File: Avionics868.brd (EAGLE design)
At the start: 88.8 x 22.9 mm, 65 parts, among them SW1 B3U-1000P-2P-SMD, U1 ATSAMD21G18_QFN, U2 SPX3819M5-L-3-0, U3 MCP73831T-2ACI/OT, U4 MPU-9250, U5 SIM868, U6 BMP280, X1 JSTPH, X2 32.768, X3 ST-USB-001G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

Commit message: a ground via was unconnected
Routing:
- net GND: track 309.9 -> 310.7 mm
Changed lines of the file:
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@@
 <wire x1="46.5455" y1="11.43" x2="46.5045" y2="11.4325" width="0" layer="19" extent="1-1"/>
 <wire x1="17.399" y1="5.715" x2="17.526" y2="4.0005" width="0" layer="19" extent="1-1"/>
+<wire x1="2.413" y1="11.43" x2="1.5875" y2="11.43" width="0.8128" layer="1"/>
 </signal>
 <signal name="MOSI">

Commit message: Made lots of tweaks!
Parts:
- removed GPS_ANT, GSM_ANT: U-FL, Seeed-Connector -2016:U-FL3P-SMD-2.6X2.6X1.0MM
- added C25: 100nf, Seeed-Capacitor-2016:C0603
- added C26: 10nf, Seeed-Capacitor-2016:C0603
- added C27, C28, C29: 10uf, Seeed-Capacitor-2016:C0603
- added X5, X6: U-FL, Seeed-Connector -2016:U-FL3P-SMD-2.6X2.6X1.0MM
- C1, C14, C7: value 1uF -> 1uf; device microbuilder:0603-NO -> Seeed-Capacitor-2016:C0603
- C10, C11, C12, C13, C9: device Seeed-Capacitor-2016:C0402 -> Seeed-Capacitor-2016:C0603
- C15: device Seeed-Capacitor-2016:C0402 -> Custom:C0603
- C19, C22, C24: value 100nf -> 10nf; device Seeed-Capacitor-2016:C0402 -> Seeed-Capacitor-2016:C0603
- C2, C4: value 22pF -> 22pf; device microbuilder:0603-NO -> Seeed-Capacitor-2016:C0603
- C21, C23: value 10uf -> 100nf
- R3, R4, R5, R9: device Seeed-Resistor-2016:R0402 -> Seeed-Resistor-2016:R0603
- moved C24 113.9 mm to (-21.6, -15.2)
- moved C22 111.2 mm to (-21.6, -26.7), turned to 0 degrees
- moved C23 110.5 mm to (-21.6, -11.4), turned to 0 degrees
- moved C21 100.4 mm to (-21.6, -22.9)
- moved C20 29.3 mm to (65.7, 27.2), turned to 270 degrees
- moved U4 28.6 mm to (65.8, 30.1)
- moved C9 27.6 mm to (62.2, 27.9), turned to 90 degrees
- moved C10 27.1 mm to (62.2, 31.6), turned to 90 degrees
- moved C11 27.1 mm to (62.0, 29.9), turned to 90 degrees
- moved R4 19.9 mm to (56.5, 32.3)
- moved R5 19.5 mm to (53.3, 32.3)
- moved C13 18.8 mm to (53.2, 26.9)
- moved C19 18.8 mm to (55.4, 26.9)
- moved U6 18.8 mm to (54.4, 28.9)
- moved L2 10.0 mm to (38.2, 5.40), turned to 270 degrees
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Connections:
- net +3V: now also C20.2, C23.2, C27.2, C28.2; no longer C20.1, C23.1
- net GND: now also C20.1, C21.1, C23.1, C25.1, C26.1, C27.1, C28.1, C29.1, X5.GND1, X5.GND2, X6.GND1, X6.GND2; no longer C20.2, C21.2, C23.2, GPS_ANT.GND1, GPS_ANT.GND2, GSM_ANT.GND1, GSM_ANT.GND2
- net GPS_ANT: now also X6.D; no longer GPS_ANT.D
- net GSM_ANT: now also X5.D; no longer GSM_ANT.D
- net SIM_VDD: now also C21.2, C29.2; no longer C21.1
- net VBAT: now also C25.2, C26.2
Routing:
- net GND: track 310.7 -> 251.6 mm, vias 111 -> 66
- net TX5/GPS_RX: track 53.9 -> 25.0 mm
- net D7/SD_CS: track 81.2 -> 53.2 mm
- net GPS_EN: track 58.3 -> 33.0 mm
- net RX5/GPS_TX: track 50.1 -> 27.6 mm
- net +3V: track 172.0 -> 151.7 mm, vias 9 -> 12
- net !RESET: track 23.7 -> 11.4 mm
- net D4/TX2/GSM_RX: track 34.6 -> 22.3 mm
- net D9/VOLT: track 38.9 -> 26.6 mm, vias 5 -> 3
- net SCL: track 41.3 -> 30.7 mm, vias 2 -> 1
- net D3/RX2/GSM_TX: track 33.9 -> 29.9 mm
- net RTS2: track 38.4 -> 34.5 mm
- net SDA: track 40.9 -> 37.6 mm, vias 3 -> 1
- net PWRKEY: track 31.3 -> 28.1 mm
- net D5/CTS2: track 29.8 -> 26.8 mm
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- added copper zone on layer 16, net +3V
- removed copper zone on layer 1, net VBAT
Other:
- board size 88.8 x 22.9 mm -> 86.4 x 22.9 mm

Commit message: LOTS of tweaks. No more 403s.
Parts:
- removed C27: 10uf, Seeed-Capacitor-2016:C0603
- moved C28 103.8 mm to (80.0, 2.10), turned to 180 degrees
- moved C29 101.2 mm to (66.0, 20.3)
- moved C21 101.2 mm to (69.9, 20.3)
- moved C22 101.1 mm to (67.9, 20.3)
- moved C23 100.6 mm to (78.1, 2.10), turned to 180 degrees
- moved C24 99.3 mm to (76.2, 2.10), turned to 180 degrees
- moved C26 64.8 mm to (46.1, 11.4), turned to 90 degrees
- moved C25 58.2 mm to (41.7, 18.8), turned to 180 degrees
- moved C11 30.4 mm to (36.1, 13.9)
- moved C10 30.0 mm to (36.8, 15.6)
- moved U4 29.6 mm to (40.8, 14.4)
- moved C20 29.2 mm to (41.1, 11.6)
- moved C9 29.2 mm to (38.6, 10.8), turned to 180 degrees
- moved R5 27.8 mm to (32.2, 14.3), turned to 0 degrees
- moved R4 24.5 mm to (46.8, 9.72)
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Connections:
- net +3V: no longer C27.2
- net GND: no longer C27.1
- net SIM_CLK: now also D3.1; no longer D3.4
- net SIM_DATA: now also D3.3; no longer D3.5
- net SIM_RST: now also D3.5; no longer D3.3
- net SIM_VDD: now also D3.4; no longer D3.1
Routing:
- net D7/SD_CS: track 53.2 -> 78.4 mm
- net TX5/GPS_RX: track 25.0 -> 47.5 mm
- net GPS_EN: track 33.0 -> 52.2 mm
- net MOSI: track 77.1 -> 57.9 mm
- net RX5/GPS_TX: track 27.6 -> 46.6 mm
- net SCL: track 30.7 -> 47.8 mm, vias 1 -> 2
- net SCK: track 73.2 -> 58.3 mm
- net !RESET: track 11.4 -> 23.7 mm
- net SIM_CLK: track 19.3 -> 30.9 mm
- net D9/VOLT: track 26.6 -> 36.6 mm
- net D4/TX2/GSM_RX: track 22.3 -> 31.9 mm
- net SDA: track 37.6 -> 46.9 mm, vias 1 -> 5
- net MISO: track 67.3 -> 74.4 mm
- net EN: track 7.56 -> 12.8 mm
- net SIM_DATA: track 22.2 -> 27.2 mm
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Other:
- outline, holes or cut-outs redrawn
- board text added: "BATCH"
- board text removed: "EXPERIMENT"

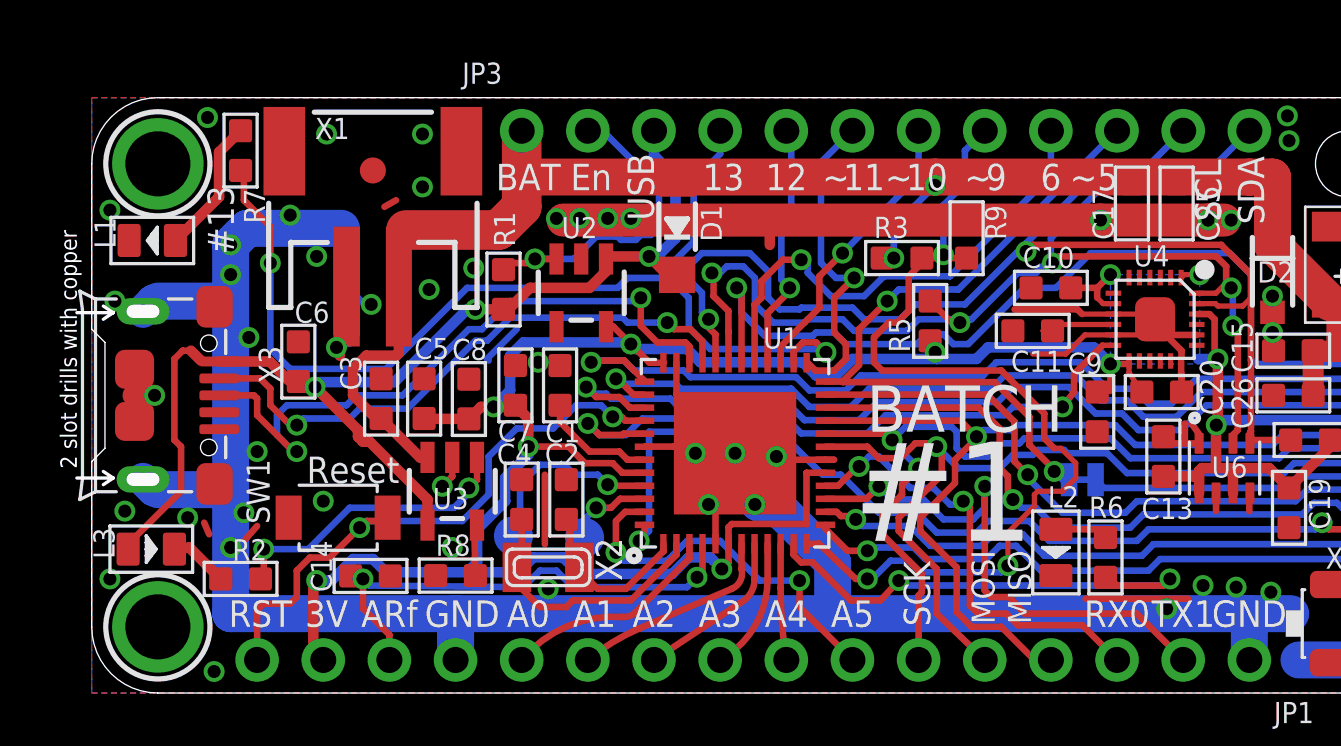
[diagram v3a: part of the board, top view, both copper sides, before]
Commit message: Swapped USB port to deegou
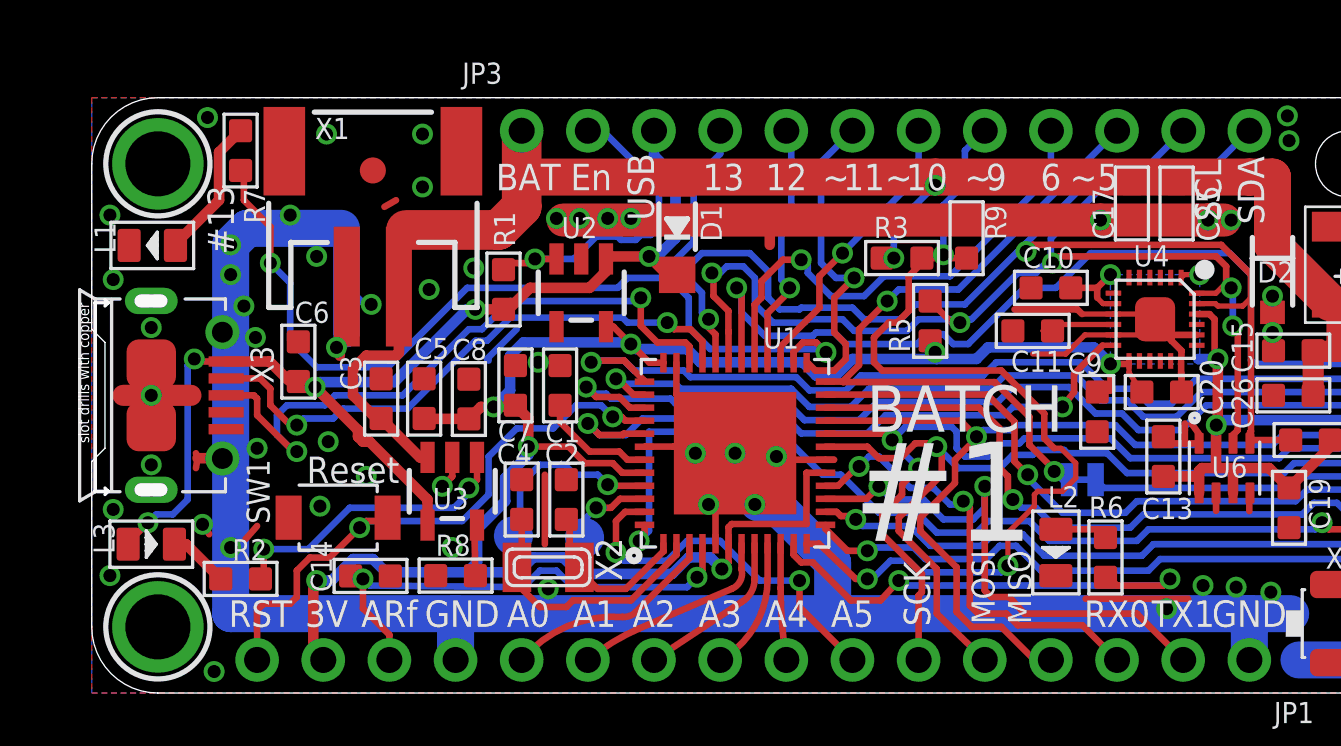
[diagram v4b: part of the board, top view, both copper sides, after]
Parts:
- X3: value ST-USB-001G -> (none); device Seeed-Connector -2016:MICRO-USB5+4P-SMD-0.65-B -> Deegou-Connectors:MICRO-USB5+6P-SMD-0.65-AB
- moved X3 2.86 mm to (2.29, 11.4)
- moved L1 0.19 mm to (2.33, 17.2)
- moved L3 0.19 mm to (2.29, 5.71)
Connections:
- net GND: now also X3.P1, X3.P2, X3.P3, X3.P4, X3.P5, X3.P6; no longer X3.S1, X3.S2, X3.S3, X3.S4, X3.S5, X3.S6
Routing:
- net GND: track 255.3 -> 251.6 mm, vias 66 -> 70
- net VBUS: track 44.0 -> 43.3 mm, vias 3 -> 5
- net D13/RLED: track 40.7 -> 40.0 mm

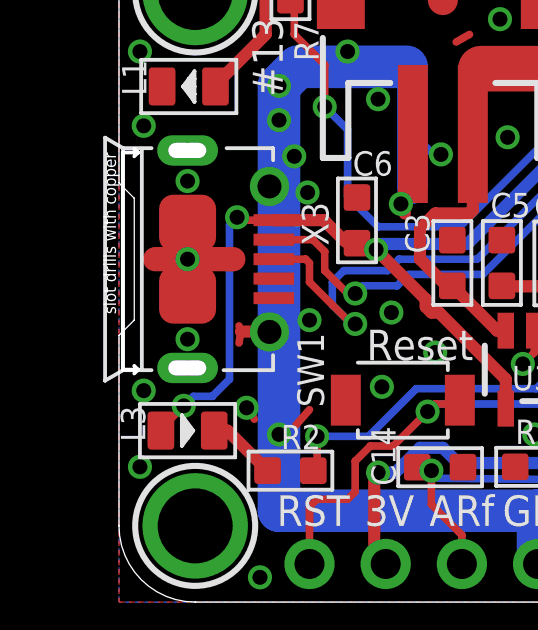
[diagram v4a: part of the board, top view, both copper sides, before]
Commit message: added seeed MPN as attribute on Deegou USB port
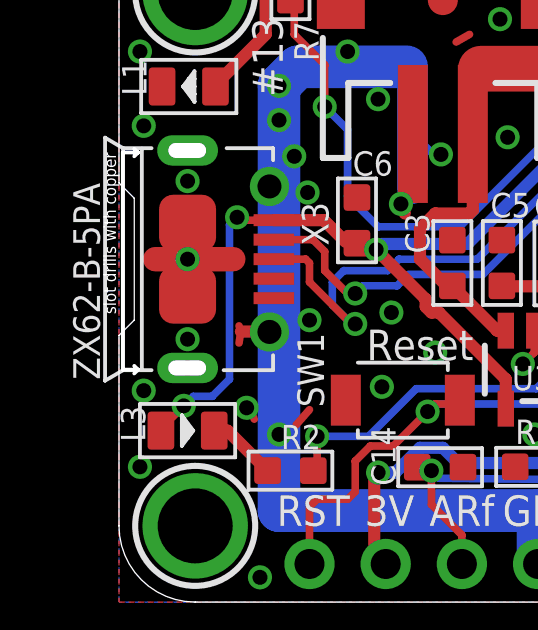
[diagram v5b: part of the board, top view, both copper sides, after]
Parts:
- X3: value (none) -> ZX62-B-5PA
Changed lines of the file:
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@@
 <attribute name="NAME" x="65.7225" y="21.5265" size="0.635" layer="33" ratio="10" rot="R270"/>
 </element>
-<element name="X3" library="Deegou-Connectors" package="MICRO-USB5+6P-SMD-0.65-AB" value="" x="2.286" y="11.43" rot="R270">
+<element name="X3" library="Deegou-Connectors" package="MICRO-USB5+6P-SMD-0.65-AB" value="ZX62-B-5PA" x="2.286" y="11.43" rot="R270">
 <attribute name="MFR" value="Generic" x="2.286" y="11.43" size="1.778" layer="27" rot="R270" display="off"/>
 <attribute name="MPN" value="AO1SB141B1-067" x="2.286" y="11.43" size="1.778" layer="27" rot="R270" display="off"/>
+<attribute name="SEEED" value="ZX62-B-5PA" x="2.286" y="11.43" size="1.778" layer="27" rot="R270" display="off"/>
 </element>
 </elements>

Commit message: removed wattages in resistor values
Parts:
- R1: value 100K 1/10W -> 100K
- R2, R6, R7: value 1K 1/10W -> 1K
- R8: value 10K 1/10W -> 10K
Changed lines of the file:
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@@
 <attribute name="MPN" value="CC0603KRX7R8BB105" x="10.70490625" y="4.4958" size="1.778" layer="27" rot="R90" display="off"/>
 </element>
-<element name="R7" library="Seeed-Resistor-2016" package="R0603" value="1K 1/10W" x="5.715" y="20.828" smashed="yes" rot="R180">
+<element name="R7" library="Seeed-Resistor-2016" package="R0603" value="1K" x="5.715" y="20.828" smashed="yes" rot="R180">
 <attribute name="NAME" x="5.842" y="19.3675" size="0.8128" layer="25" ratio="18" rot="R270"/>
 <attribute name="VALUE" value="1K 1/10W" x="8.636" y="20.701" size="0.8128" layer="27" ratio="10"/>
@@
 <attribute name="MPN" value="EL-17-215/BHC-AN1P2/3T" x="2.286" y="5.715" size="1.778" layer="27" display="off"/>
 </element>
-<element name="R2" library="Seeed-Resistor-2016" package="R0603" value="1K 1/10W" x="5.715" y="4.3815" smashed="yes" rot="R90">
+<element name="R2" library="Seeed-Resistor-2016" package="R0603" value="1K" x="5.715" y="4.3815" smashed="yes" rot="R90">
 <attribute name="NAME" x="6.731" y="5.9055" size="0.8128" layer="25" font="vector" ratio="18" rot="R180"/>
 <attribute name="VALUE" value="1K 1/10W" x="7.239" y="3.6195" size="0.8128" layer="27" font="vector" ratio="10" rot="R90"/>
@@
 <attribute name="MPN" value="CC0603KRX5R6BB106" x="11.1125" y="11.303" size="1.778" layer="27" rot="R180" display="off"/>
 </element>
-<element name="R8" library="Seeed-Resistor-2016" package="R0603" value="10K 1/10W" x="13.97" y="4.5085" smashed="yes" rot="R270">
+<element name="R8" library="Seeed-Resistor-2016" package="R0603" value="10K" x="13.97" y="4.5085" smashed="yes" rot="R270">
 <attribute name="NAME" x="13.208" y="5.2705" size="0.8128" layer="25" font="vector" ratio="18"/>
 <attribute name="VALUE" value="10K 1/10W" x="14.859" y="5.7785" size="0.8128" layer="27" font="vector" ratio="10" rot="R270"/>
@@
 <attribute name="VALUE" x="17.78" y="5.334" size="0.4064" layer="28" ratio="10" rot="MR0"/>
 </element>
-<element name="R1" library="Seeed-Resistor-2016" package="R0603" value="100K 1/10W" x="15.8115" y="15.494" smashed="yes" rot="R180">
+<element name="R1" library="Seeed-Resistor-2016" package="R0603" value="100K" x="15.8115" y="15.494" smashed="yes" rot="R180">
 <attribute name="NAME" x="16.256" y="17.145" size="0.8128" layer="25" font="vector" ratio="18" rot="R90"/>
 <attribute name="VALUE" value="100K 1/10W" x="17.3355" y="14.605" size="0.8128" layer="27" font="vector" ratio="10" rot="R180"/>
@@
 <attribute name="MPN" value="17-215SYGC/S530-E2/TR8" x="37.0205" y="5.3975" size="1.778" layer="27" rot="R270" display="off"/>
 </element>
-<element name="R6" library="Seeed-Resistor-2016" package="R0603" value="1K 1/10W" x="38.9255" y="5.207" smashed="yes" rot="R180">
+<element name="R6" library="Seeed-Resistor-2016" package="R0603" value="1K" x="38.9255" y="5.207" smashed="yes" rot="R180">
 <attribute name="NAME" x="38.2905" y="6.731" size="0.8128" layer="25" font="vector" ratio="18"/>
 <attribute name="VALUE" value="1K 1/10W" x="37.1475" y="5.969" size="0.4064" layer="27" font="vector" ratio="10" rot="R180"/>
